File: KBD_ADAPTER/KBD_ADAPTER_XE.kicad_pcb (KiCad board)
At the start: 2 copper layers, 61.5 x 19.3 mm, 2 parts, among them J1 Conn_01x24, J2 Conn_02x17_Counter_Clockwise

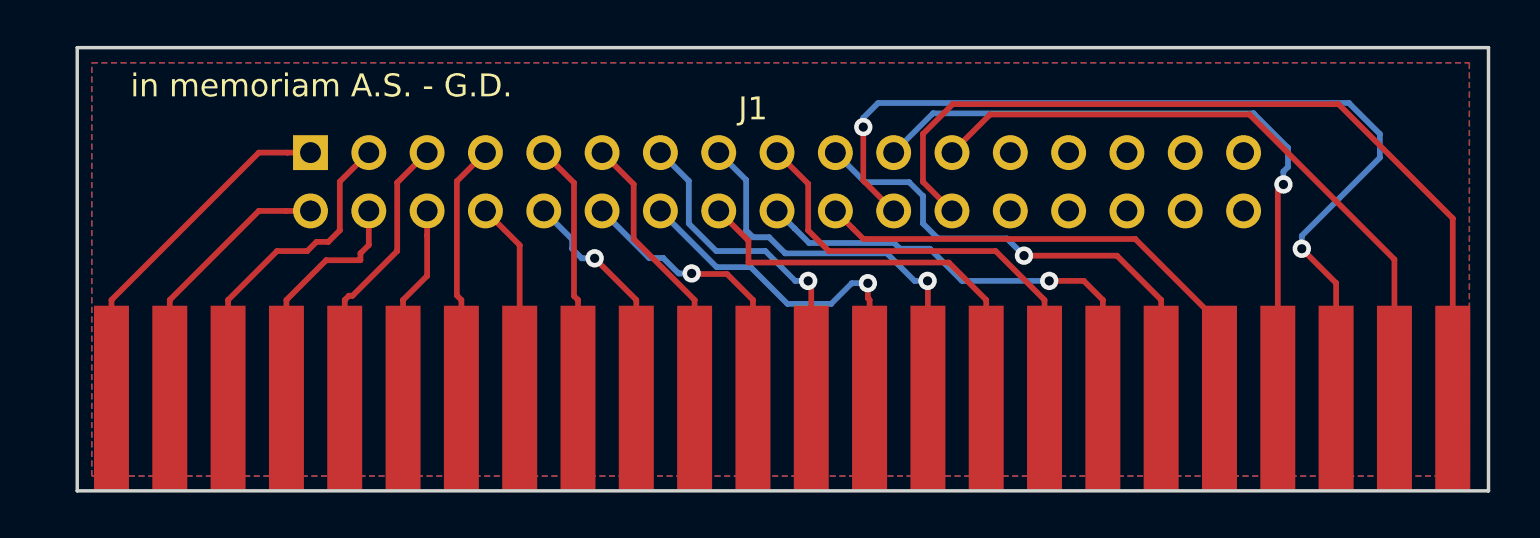
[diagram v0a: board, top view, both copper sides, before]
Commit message: It was too big. With a paper board it was too near the keyboard assy. Now it's as small as possible.
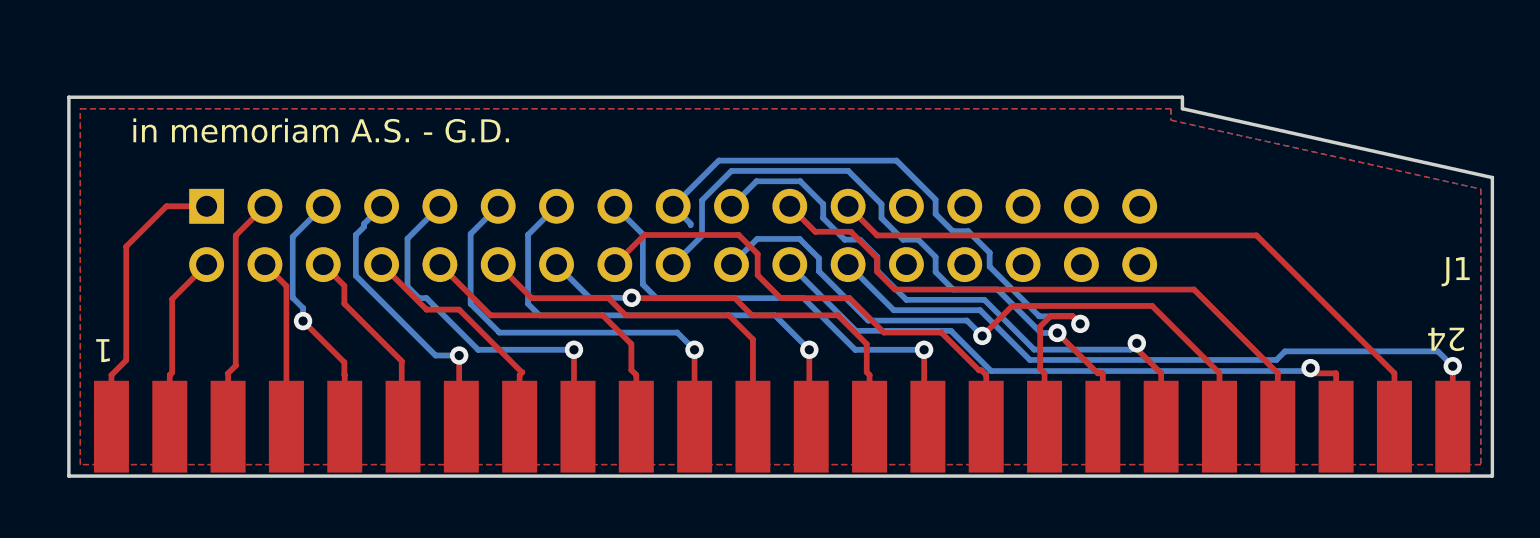
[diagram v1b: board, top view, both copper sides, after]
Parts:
- moved J2 5.09 mm to (119.0, 100.2)
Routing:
- net SELECT: track 41.4 -> 28.2 mm, vias 2 -> 1
- net IN_0: track 19.7 -> 29.9 mm, vias 0 -> 1
- net OUT_0: track 20.0 -> 28.0 mm
- net IN_1: track 12.3 -> 18.7 mm, vias 0 -> 1
- net OUT_1: track 15.0 -> 21.2 mm
- net RESET: track 37.4 -> 31.1 mm, vias 0 -> 1
- net RSC: track 22.0 -> 27.9 mm, vias 0 -> 1
- net IN_7: track 11.3 -> 15.9 mm, vias 0 -> 1
- net J_LED: track 12.0 -> 7.72 mm
- net IN_4: track 21.8 -> 26.0 mm
- net GND: track 14.3 -> 10.3 mm
- net IN_3: track 18.1 -> 22.0 mm
- net OUT_6: track 12.4 -> 16.2 mm, vias 1 -> 0
- net IN_5: track 10.1 -> 13.5 mm, vias 1 -> 0
- net VCC: track 15.6 -> 12.3 mm
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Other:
- board size 61.5 x 19.3 mm -> 62 x 16.5 mm
- board text added: "1"
- board text added: "24"
- board text added: "ATARI XL/XE keyboard adapter by RetroBitLab Tech Guy"
- board text removed: "ATARI XE keyboard adapter by RetroBitLab Tech Guy"
